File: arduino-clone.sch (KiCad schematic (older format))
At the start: 7 parts

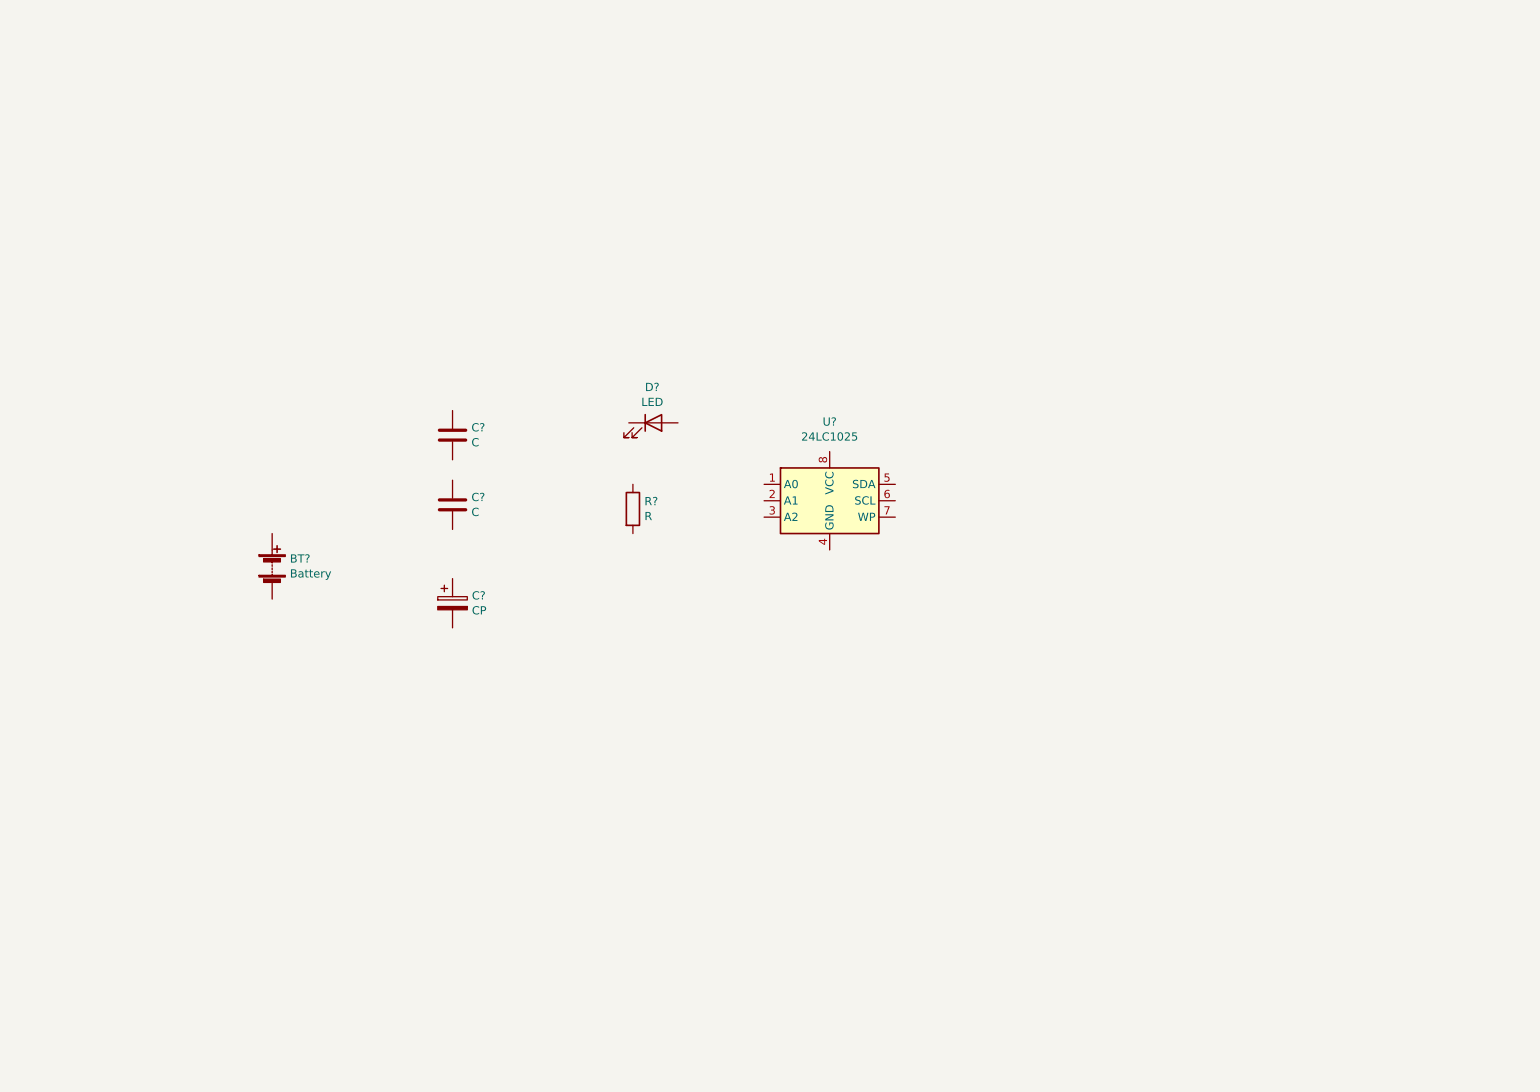
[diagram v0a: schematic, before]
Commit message: [eeschema] add heir sheet, associate footprints
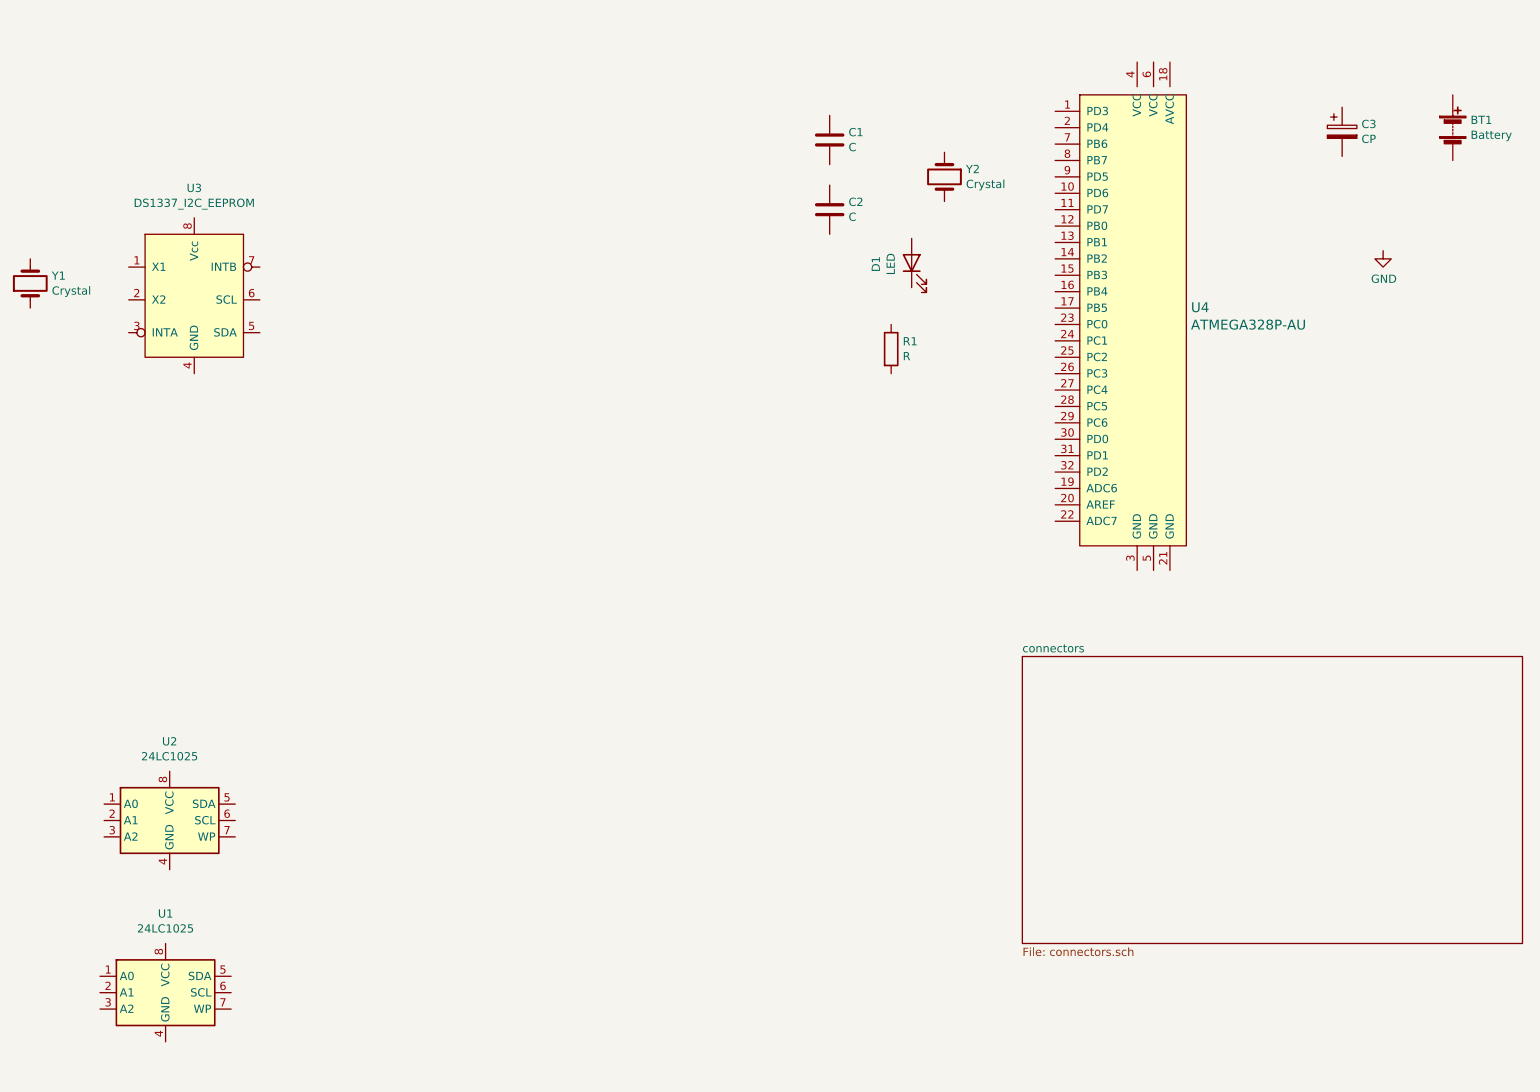
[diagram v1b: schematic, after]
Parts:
- added U1: 24LC1025, Package_SO:SOIJ-8_5.3x5.3mm_P1.27mm, symbol Memory_EEPROM:24LC1025
- added U3: DS1337_I2C_EEPROM, Package_SO:SO-8_5.3x6.2mm_P1.27mm, symbol mylib:DS1337_I2C_EEPROM
- added U4: ATMEGA328P-AU, digikey-footprints:TQFP-32_7x7mm, symbol dk_Embedded-Microcontrollers:ATMEGA328P-AU
- added Y1, Y2: Crystal, Crystal:Crystal_SMD_MicroCrystal_CC7V-T1A-2Pin_3.2x1.5mm_HandSoldering, symbol Device:Crystal
- BT1: renamed from BT?; footprint (none) -> Connector_PinHeader_2.54mm:PinHeader_1x02_P2.54mm_Vertical
- C1, C2, C3: renamed from C?; footprint (none) -> Capacitor_SMD:C_0805_2012Metric_Pad1.15x1.40mm_HandSolder
- D1: renamed from D?; footprint (none) -> LED_SMD:LED_0805_2012Metric_Pad1.15x1.40mm_HandSolder
- R1: renamed from R?; footprint (none) -> Resistor_SMD:R_0805_2012Metric_Pad1.15x1.40mm_HandSolder
- U2: renamed from U?; footprint (none) -> Package_SO:SOIJ-8_5.3x5.3mm_P1.27mm
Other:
- moved on the sheet: BT1, C1, C2, C3, D1, R1, U2
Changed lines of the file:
@@
 $Descr A4 11693 8268
 encoding utf-8
-Sheet 1 1
+Sheet 1 2
 Title "Arduino-Clone"
 Date "2020-06-14"
@@
 $EndDescr
 $Comp
-L Device:Battery BT?
+L Device:Battery BT1
 U 1 1 5EE57074
-P 3300 4000
-F 0 "BT?" H 3408 4046 50  0000 L CNN
-F 1 "Battery" H 3408 3955 50  0000 L CNN
-F 2 "" V 3300 4060 50  0001 C CNN
-F 3 "~" V 3300 4060 50  0001 C CNN
-	1    3300 4000
+P 10500 1325
+F 0 "BT1" H 10608 1371 50  0000 L CNN
+F 1 "Battery" H 10608 1280 50  0000 L CNN
+F 2 "Connector_PinHeader_2.54mm:PinHeader_1x02_P2.54mm_Vertical" V 10500 1385 50  0001 C CNN
+F 3 "~" V 10500 1385 50  0001 C CNN
+	1    10500 1325
 	1    0    0    -1
 $EndComp
 $Comp
-L Device:C C?
+L Device:C C2
 U 1 1 5EE573CD
-P 4400 3625
-F 0 "C?" H 4515 3671 50  0000 L CNN
-F 1 "C" H 4515 3580 50  0000 L CNN
-F 2 "" H 4438 3475 50  0001 C CNN
-F 3 "~" H 4400 3625 50  0001 C CNN
-	1    4400 3625
+P 6700 1825
+F 0 "C2" H 6815 1871 50  0000 L CNN
+F 1 "C" H 6815 1780 50  0000 L CNN
+F 2 "Capacitor_SMD:C_0805_2012Metric_Pad1.15x1.40mm_HandSolder" H 6738 1675 50  0001 C CNN
+F 3 "~" H 6700 1825 50  0001 C CNN
+	1    6700 1825
 	1    0    0    -1
 $EndComp
 $Comp
-L Device:CP C?
+L Device:CP C3
 U 1 1 5EE5773A
-P 4400 4225
-F 0 "C?" H 4518 4271 50  0000 L CNN
-F 1 "CP" H 4518 4180 50  0000 L CNN
-F 2 "" H 4438 4075 50  0001 C CNN
-F 3 "~" H 4400 4225 50  0001 C CNN
-	1    4400 4225
+P 9825 1350
+F 0 "C3" H 9943 1396 50  0000 L CNN
+F 1 "CP" H 9943 1305 50  0000 L CNN
+F 2 "Capacitor_SMD:C_0805_2012Metric_Pad1.15x1.40mm_HandSolder" H 9863 1200 50  0001 C CNN
+F 3 "~" H 9825 1350 50  0001 C CNN
+	1    9825 1350
 	1    0    0    -1
 $EndComp
 $Comp
-L Device:C C?
+L Device:C C1
 U 1 1 5EE57A14
-P 4400 3200
-F 0 "C?" H 4515 3246 50  0000 L CNN
-F 1 "C" H 4515 3155 50  0000 L CNN
-F 2 "" H 4438 3050 50  0001 C CNN
-F 3 "~" H 4400 3200 50  0001 C CNN
-	1    4400 3200
+P 6700 1400
+F 0 "C1" H 6815 1446 50  0000 L CNN
+F 1 "C" H 6815 1355 50  0000 L CNN
+F 2 "Capacitor_SMD:C_0805_2012Metric_Pad1.15x1.40mm_HandSolder" H 6738 1250 50  0001 C CNN
+F 3 "~" H 6700 1400 50  0001 C CNN
+	1    6700 1400
 	1    0    0    -1
 $EndComp
 $Comp
-L Device:LED D?
+L Device:LED D1
 U 1 1 5EE57CDF
-P 5625 3125
-F 0 "D?" H 5618 3342 50  0000 C CNN
-F 1 "LED" H 5618 3251 50  0000 C CNN
-F 2 "" H 5625 3125 50  0001 C CNN
-F 3 "~" H 5625 3125 50  0001 C CNN
-	1    5625 3125
+P 7200 2150
+F 0 "D1" H 7193 2367 50  0000 C CNN
+F 1 "LED" H 7193 2276 50  0000 C CNN
+F 2 "LED_SMD:LED_0805_2012Metric_Pad1.15x1.40mm_HandSolder" H 7200 2150 50  0001 C CNN
+F 3 "~" H 7200 2150 50  0001 C CNN
+	1    7200 2150
+	0    -1   -1   0
+$EndComp
+$Comp
+L Device:R R1
+U 1 1 5EE581EB
+P 7075 2675
+F 0 "R1" H 7145 2721 50  0000 L CNN
+F 1 "R" H 7145 2630 50  0000 L CNN
+F 2 "Resistor_SMD:R_0805_2012Metric_Pad1.15x1.40mm_HandSolder" V 7005 2675 50  0001 C CNN
+F 3 "~" H 7075 2675 50  0001 C CNN
+	1    7075 2675
 	1    0    0    -1
 $EndComp
 $Comp
-L Device:R R?
-U 1 1 5EE581EB
-P 5500 3650
-F 0 "R?" H 5570 3696 50  0000 L CNN
-F 1 "R" H 5570 3605 50  0000 L CNN
-F 2 "" V 5430 3650 50  0001 C CNN
-F 3 "~" H 5500 3650 50  0001 C CNN
-	1    5500 3650
+L Memory_EEPROM:24LC1025 U2
+U 1 1 5EE58CDC
+P 2675 5550
+F 0 "U2" H 2675 6031 50  0000 C CNN
+F 1 "24LC1025" H 2675 5940 50  0000 C CNN
+F 2 "Package_SO:SOIJ-8_5.3x5.3mm_P1.27mm" H 2675 5550 50  0001 C CNN
+F 3 "http://ww1.microchip.com/downloads/en/DeviceDoc/21941B.pdf" H 2675 5550 50  0001 C CNN
+	1    2675 5550
+	1    0    0    -1
+$EndComp
+$Sheet
+S 7875 4550 3050 1750
+U 5EE59D89
+F0 "connectors" 50
+F1 "connectors.sch" 50
+$EndSheet
+$Comp
+L dk_Embedded-Microcontrollers:ATMEGA328P-AU U4
+U 1 1 5EE5B69B
+P 8575 2525
+F 0 "U4" H 8903 2628 60  0000 L CNN
+F 1 "ATMEGA328P-AU" H 8903 2522 60  0000 L CNN
+F 2 "digikey-footprints:TQFP-32_7x7mm" H 8775 2725 60  0001 L CNN
+F 3 "http://www.microchip.com/mymicrochip/filehandler.aspx?ddocname=en608326" H 8775 2825 60  0001 L CNN
+F 4 "ATMEGA328P-AU-ND" H 8775 2925 60  0001 L CNN "Digi-Key_PN"
+F 5 "ATMEGA328P-AU" H 8775 3025 60  0001 L CNN "MPN"
+F 6 "Integrated Circuits (ICs)" H 8775 3125 60  0001 L CNN "Category"
+F 7 "Embedded - Microcontrollers" H 8775 3225 60  0001 L CNN "Family"
+F 8 "http://www.microchip.com/mymicrochip/filehandler.aspx?ddocname=en608326" H 8775 3325 60  0001 L CNN "DK_Datasheet_Link"
+F 9 "/product-detail/en/microchip-technology/ATMEGA328P-AU/ATMEGA328P-AU-ND/1832260" H 8775 3425 60  0001 L CNN "DK_Detail_Page"
+F 10 "IC MCU 8BIT 32KB FLASH 32TQFP" H 8775 3525 60  0001 L CNN "Description"
+F 11 "Microchip Technology" H 8775 3625 60  0001 L CNN "Manufacturer"
+F 12 "Active" H 8775 3725 60  0001 L CNN "Status"
+	1    8575 2525
 	1    0    0    -1
 $EndComp
 $Comp
-L Memory_EEPROM:24LC1025 U?
-U 1 1 5EE58CDC
-P 6700 3600
-F 0 "U?" H 6700 4081 50  0000 C CNN
-F 1 "24LC1025" H 6700 3990 50  0000 C CNN
-F 2 "" H 6700 3600 50  0001 C CNN
-F 3 "http://ww1.microchip.com/downloads/en/DeviceDoc/21941B.pdf" H 6700 3600 50  0001 C CNN
-	1    6700 3600
+L mylib:DS1337_I2C_EEPROM U3
+U 1 1 5EE60820
+P 2825 2325
+F 0 "U3" H 2825 2956 50  0000 C CNN
+F 1 "DS1337_I2C_EEPROM" H 2825 2865 50  0000 C CNN
+F 2 "Package_SO:SO-8_5.3x6.2mm_P1.27mm" H 2675 2175 50  0001 C CNN
+F 3 "https://datasheets.maximintegrated.com/en/ds/DS1337-DS1337C.pdf" H 2675 2175 50  0001 C CNN
+	1    2825 2325
 	1    0    0    -1
 $EndComp
+$Comp
+L Device:Crystal Y1
+U 1 1 5EE6178D
+P 1825 2275
+F 0 "Y1" V 1871 2144 50  0000 R CNN
+F 1 "Crystal" V 1780 2144 50  0000 R CNN
+F 2 "Crystal:Crystal_SMD_MicroCrystal_CC7V-T1A-2Pin_3.2x1.5mm_HandSoldering" H 1825 2275 50  0001 C CNN
+F 3 "~" H 1825 2275 50  0001 C CNN
+	1    1825 2275
+	0    -1   -1   0
+$EndComp
+$Comp
+L Device:Crystal Y2
+U 1 1 5EE61E61
+P 7400 1625
+F 0 "Y2" V 7354 1756 50  0000 L CNN
+F 1 "Crystal" V 7445 1756 50  0000 L CNN
+F 2 "Crystal:Crystal_SMD_MicroCrystal_CC7V-T1A-2Pin_3.2x1.5mm_HandSoldering" H 7400 1625 50  0001 C CNN
+F 3 "~" H 7400 1625 50  0001 C CNN
+	1    7400 1625
+	0    1    1    0
+$EndComp
+$Comp
+L Memory_EEPROM:24LC1025 U1
+U 1 1 5EE633DF
+P 2650 6600
+F 0 "U1" H 2650 7081 50  0000 C CNN
+F 1 "24LC1025" H 2650 6990 50  0000 C CNN
+F 2 "Package_SO:SOIJ-8_5.3x5.3mm_P1.27mm" H 2650 6600 50  0001 C CNN
+F 3 "http://ww1.microchip.com/downloads/en/DeviceDoc/21941B.pdf" H 2650 6600 50  0001 C CNN
+	1    2650 6600
+	1    0    0    -1
+$EndComp
+$Comp
+L power:GND #PWR0101
+U 1 1 5EE677A2
+P 10075 2075
+F 0 "#PWR0101" H 10075 1825 50  0001 C CNN
+F 1 "GND" H 10080 1902 50  0000 C CNN
+F 2 "" H 10075 2075 50  0001 C CNN
+F 3 "" H 10075 2075 50  0001 C CNN
+	1    10075 2075
+	1    0    0    -1
+$EndComp

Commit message: [eeshema] assign values, connect symbols
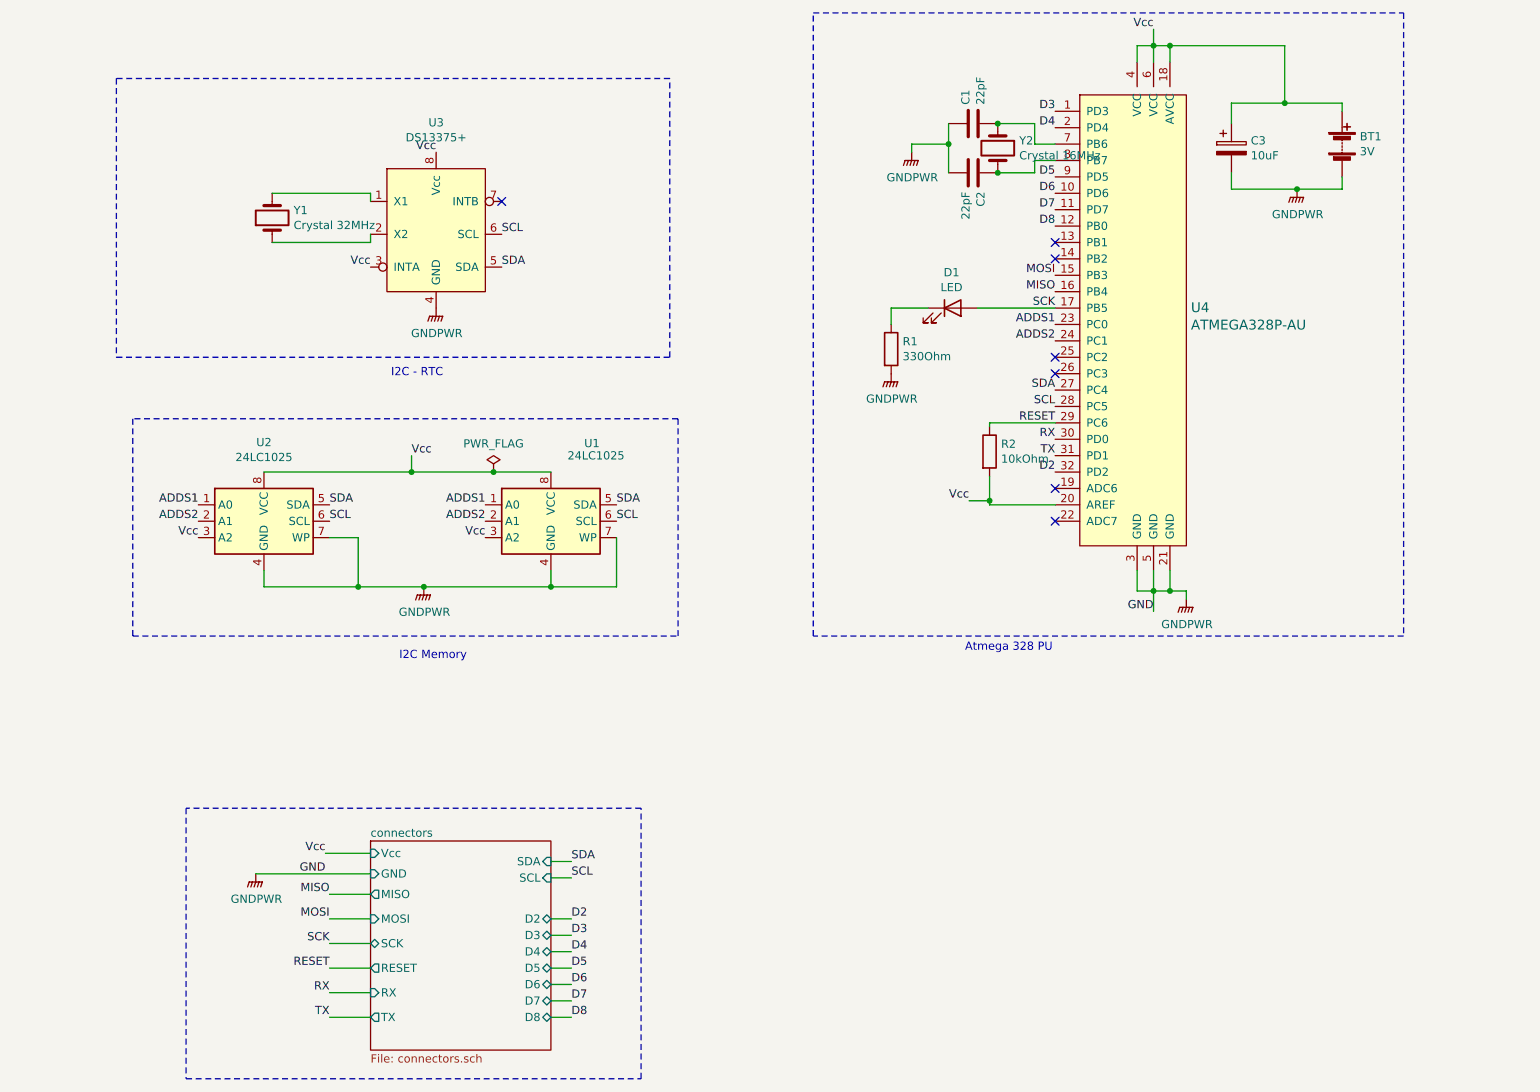
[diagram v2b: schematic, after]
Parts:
- added R2: 10kOhm, Resistor_SMD:R_0805_2012Metric_Pad1.15x1.40mm_HandSolder, symbol Device:R
- BT1: value Battery -> 3V
- C1, C2: value C -> 22pF
- C3: value CP -> 10uF
- R1: value R -> 330Ohm
- U3: value DS1337_I2C_EEPROM -> DS13375+
- Y1: value Crystal -> Crystal 32MHz
- Y2: value Crystal -> Crystal 16MHz
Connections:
- net Vcc: now reaches BT1.1 (+)
- net Vcc: now also C3.1, U1.3 (A2), U1.8 (VCC), U2.3 (A2), U2.8 (VCC), U3.3 (INTA), U3.8 (Vcc), U4.18 (AVCC), U4.20 (AREF), U4.4 (VCC), U4.6 (VCC), R2.2
- net GNDPWR: now reaches BT1.2 (-)
- net GNDPWR: now also C1.1, C2.2, C3.2, R1.2, U1.4 (GND), U1.7 (WP), U2.4 (GND), U2.7 (WP), U3.4 (GND), U4.21 (GND), U4.3 (GND), U4.5 (GND)
- net at C2.1: now also U4.8 (PB7), Y2.2
- net at C1.2: now also U4.7 (PB6), Y2.1
- net at D1.1 (K): now also R1.1
- net SCK: now reaches D1.2 (A)
- net SCK: now also U4.17 (PB5)
- net ADDS1: now reaches U2.1 (A0)
- net ADDS1: now also U1.1 (A0), U4.23 (PC0)
- net ADDS2: now reaches U2.2 (A1)
- net ADDS2: now also U1.2 (A1), U4.24 (PC1)
- net SDA: now reaches U2.5 (SDA)
- net SDA: now also U1.5 (SDA), U3.5 (SDA), U4.27 (PC4)
- net SCL: now reaches U2.6 (SCL)
- net SCL: now also U1.6 (SCL), U3.6 (SCL), U4.28 (PC5)
- net D3: now reaches U4.1 (PD3)
- net D6: now reaches U4.10 (PD6)
- net D7: now reaches U4.11 (PD7)
- net D8: now reaches U4.12 (PB0)
- net MOSI: now reaches U4.15 (PB3)
- net MISO: now reaches U4.16 (PB4)
- net D4: now reaches U4.2 (PD4)
- net RESET: now reaches U4.29 (PC6)
- net RESET: now also R2.1
- net RX: now reaches U4.30 (PD0)
- net TX: now reaches U4.31 (PD1)
- net D2: now reaches U4.32 (PD2)
- net D5: now reaches U4.9 (PD5)
- net at U3.1 (X1): now also Y1.2
- net at U3.2 (X2): now also Y1.1
- no-connect marks 0 -> 7
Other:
- note added: "Atmega 328 PU"
- note added: "I2C - RTC"
- note added: "I2C Memory"
- moved on the sheet: BT1, C1, C2, C3, D1, U1, U2, U3, Y1, Y2
